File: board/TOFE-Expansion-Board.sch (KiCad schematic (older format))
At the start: 6 parts, among them U1 TOFE-8X, U7 24AA01/24LC01B

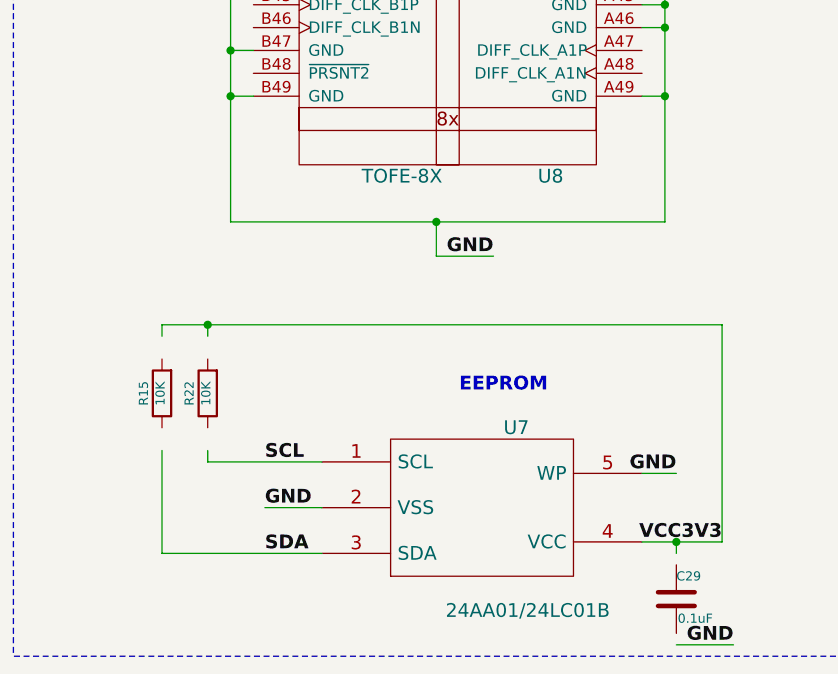
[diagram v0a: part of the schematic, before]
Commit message: Upgrading schematic to KiCad 4.0.0rc1
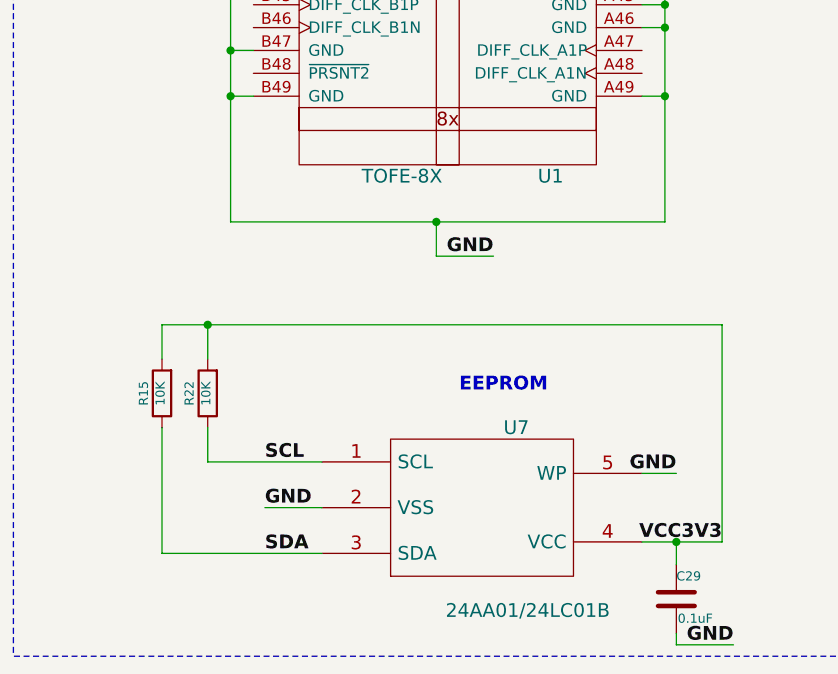
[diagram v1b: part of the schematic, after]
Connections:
- wire segments 78 -> 79
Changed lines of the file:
@@
 LIBS:EEPROM
 LIBS:TOFE-Expansion-Board-cache
-LIBS:TOFE-Expansion-Board-cache
-EELAYER 27 0
+EELAYER 25 0
 EELAYER END
 $Descr A3 16535 11693
@@
 U 1 1 561CABB0
 P 5450 5200
-F 0 "U8" H 5450 2350 60  0000 C CNN
+F 0 "U1" H 5450 2350 60  0000 C CNN
 F 1 "TOFE-8X" H 4800 2350 60  0000 C CNN
 F 2 "~" H 4150 4900 60  0000 C CNN
@@
 	5850 9650 6200 9650
 Wire Wire Line
-	3950 9300 3950 9250
-Wire Wire Line
-	3750 9250 3750 9700
-Wire Wire Line
-	3750 8750 3750 8700
+	3950 9150 3950 9300
+Wire Wire Line
+	3750 9150 3750 9700
+Wire Wire Line
+	3750 8700 3750 8850
 Wire Wire Line
 	3750 8700 6200 8700
 Wire Wire Line
-	3950 8750 3950 8700
+	3950 8700 3950 8850
 Connection ~ 3950 8700
 Wire Wire Line
 	6200 8700 6200 9650
 Wire Wire Line
-	6000 9700 6000 9650
+	6000 9650 6000 9750
 Connection ~ 6000 9650
 Wire Wire Line
@@
 Wire Wire Line
 	4150 3000 3700 3000
+Wire Wire Line
+	6000 10050 6000 10100
 $EndSCHEMATC

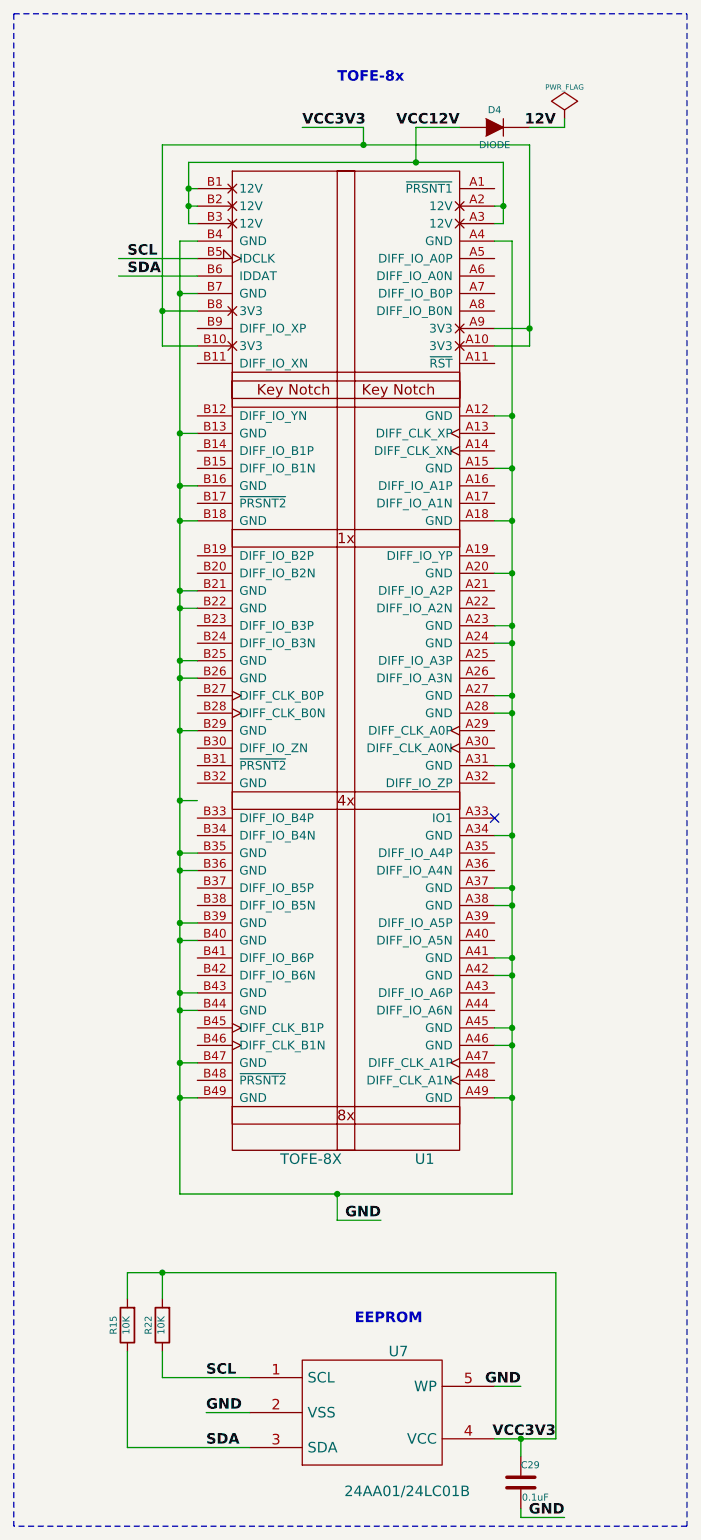
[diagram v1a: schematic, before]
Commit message: schematic: Fixing GND alignment after last change.
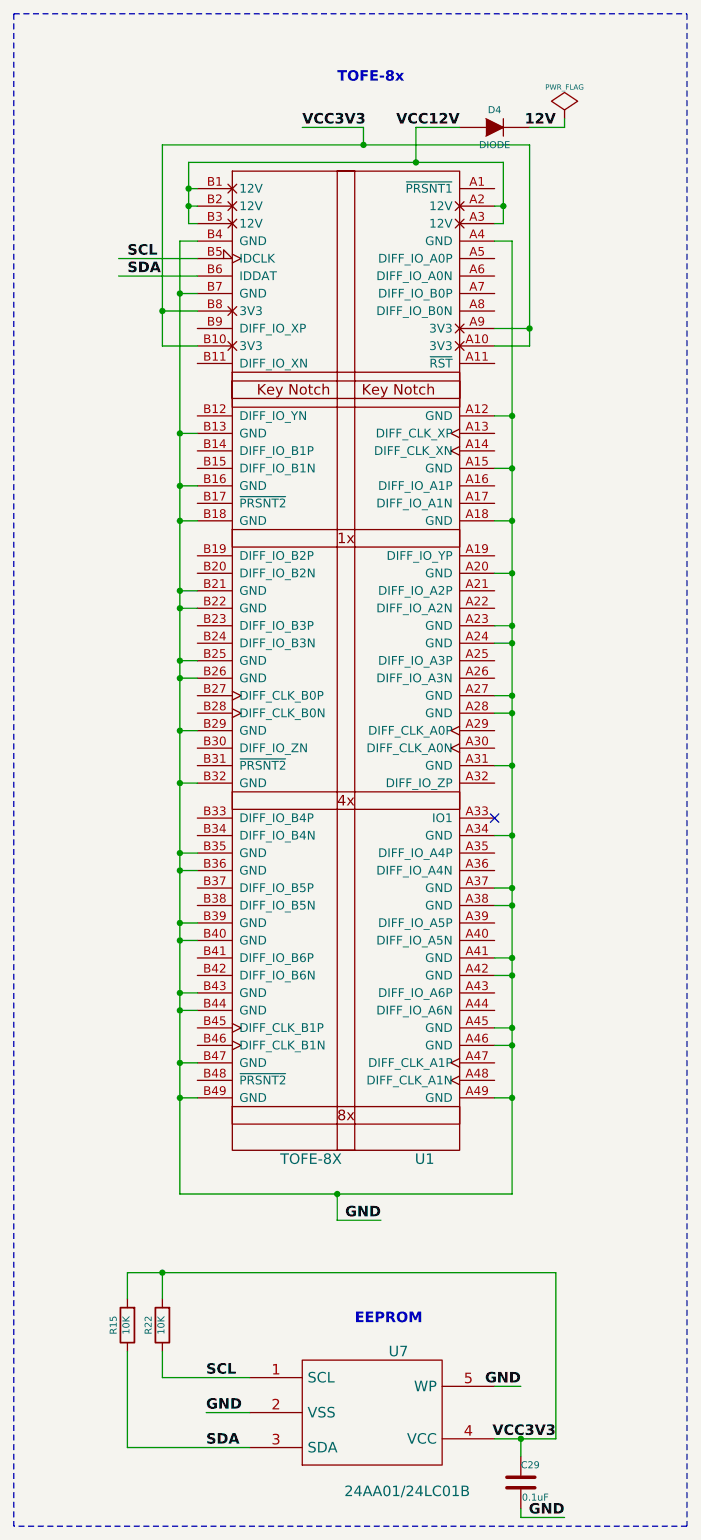
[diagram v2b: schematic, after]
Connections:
- wire segments 79 -> 124
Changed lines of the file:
@@
 	4150 2800 4050 2800
 Wire Wire Line
-	4050 2800 4050 8250
+	4050 2800 4050 3100
+Wire Wire Line
+	4050 3100 4050 3900
+Wire Wire Line
+	4050 3900 4050 4200
+Wire Wire Line
+	4050 4200 4050 4400
+Wire Wire Line
+	4050 4400 4050 4800
+Wire Wire Line
+	4050 4800 4050 4900
+Wire Wire Line
+	4050 4900 4050 5200
+Wire Wire Line
+	4050 5200 4050 5300
+Wire Wire Line
+	4050 5300 4050 5600
+Wire Wire Line
+	4050 5600 4050 5900
+Wire Wire Line
+	4050 5900 4050 6300
+Wire Wire Line
+	4050 6300 4050 6400
+Wire Wire Line
+	4050 6400 4050 6700
+Wire Wire Line
+	4050 6700 4050 6800
+Wire Wire Line
+	4050 6800 4050 7100
+Wire Wire Line
+	4050 7100 4050 7200
+Wire Wire Line
+	4050 7200 4050 7500
+Wire Wire Line
+	4050 7500 4050 7700
+Wire Wire Line
+	4050 7700 4050 8250
 Wire Wire Line
 	4050 3100 4150 3100
@@
 Connection ~ 4050 5300
 Wire Wire Line
-	4050 6000 4150 6000
+	4050 5900 4150 5900
 Connection ~ 4050 5600
 Wire Wire Line
 	4050 6300 4150 6300
-Connection ~ 4050 6000
+Connection ~ 4050 5900
 Wire Wire Line
 	4050 6400 4150 6400
@@
 Connection ~ 5950 7400
 Wire Wire Line
-	4050 8250 5950 8250
+	4050 8250 4950 8250
+Wire Wire Line
+	4950 8250 5950 8250
 Connection ~ 4050 7700
 Connection ~ 5950 7700
@@
 	3950 3400 4150 3400
 Wire Wire Line
-	3950 2250 3950 3400
+	3950 2250 3950 3200
+Wire Wire Line
+	3950 3200 3950 3400
 Wire Wire Line
 	3950 3200 4150 3200
@@
 	5850 3300 6050 3300
 Wire Wire Line
-	6050 2250 6050 3400
+	6050 2250 6050 3300
+Wire Wire Line
+	6050 3300 6050 3400
 Wire Wire Line
 	6050 3400 5850 3400
 Wire Wire Line
-	3950 2250 6050 2250
+	3950 2250 5100 2250
+Wire Wire Line
+	5100 2250 6050 2250
 Connection ~ 6050 3300
 Connection ~ 3950 3200
@@
 	4100 2700 4150 2700
 Wire Wire Line
-	4100 2350 4100 2700
+	4100 2350 4100 2500
+Wire Wire Line
+	4100 2500 4100 2600
+Wire Wire Line
+	4100 2600 4100 2700
 Wire Wire Line
 	4100 2600 4150 2600
@@
 	5900 2700 5850 2700
 Wire Wire Line
-	5900 2350 5900 2700
+	5900 2350 5900 2600
+Wire Wire Line
+	5900 2600 5900 2700
 Wire Wire Line
 	5900 2600 5850 2600
 Wire Wire Line
-	4100 2350 5900 2350
+	4100 2350 5400 2350
+Wire Wire Line
+	5400 2350 5900 2350
 Connection ~ 5900 2600
 Connection ~ 4100 2500
@@
 	6250 2150 6250 2100
 Wire Wire Line
-	5850 9650 6200 9650
+	5850 9650 6000 9650
+Wire Wire Line
+	6000 9650 6200 9650
 Wire Wire Line
 	3950 9150 3950 9300
@@
 	3750 8700 3750 8850
 Wire Wire Line
-	3750 8700 6200 8700
+	3750 8700 3950 8700
+Wire Wire Line
+	3950 8700 6200 8700
 Wire Wire Line
 	3950 8700 3950 8850
@@
 	6000 10100 6250 10100
 Wire Wire Line
-	5950 8250 5950 2800
+	5950 8250 5950 7700
+Wire Wire Line
+	5950 7700 5950 7400
+Wire Wire Line
+	5950 7400 5950 7300
+Wire Wire Line
+	5950 7300 5950 7000
+Wire Wire Line
+	5950 7000 5950 6900
+Wire Wire Line
+	5950 6900 5950 6600
+Wire Wire Line
+	5950 6600 5950 6500
+Wire Wire Line
+	5950 6500 5950 6200
+Wire Wire Line
+	5950 6200 5950 5800
+Wire Wire Line
+	5950 5800 5950 5500
+Wire Wire Line
+	5950 5500 5950 5400
+Wire Wire Line
+	5950 5400 5950 5100
+Wire Wire Line
+	5950 5100 5950 5000
+Wire Wire Line
+	5950 5000 5950 4700
+Wire Wire Line
+	5950 4700 5950 4400
+Wire Wire Line
+	5950 4400 5950 4100
+Wire Wire Line
+	5950 4100 5950 3800
+Wire Wire Line
+	5950 3800 5950 2800
 Text Label 3750 2900 0    60   ~ 12
 SCL
